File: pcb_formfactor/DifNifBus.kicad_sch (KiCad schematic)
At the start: 24 parts, among them J1 DBA-ESDI, U10 74LVC4245, U11 74LCX07, U12 74VHCT125, U14 74LVC4245, U6 74LVC4245, U7 74LVC4245, U8 74LVC4245, U9 74LVC4245

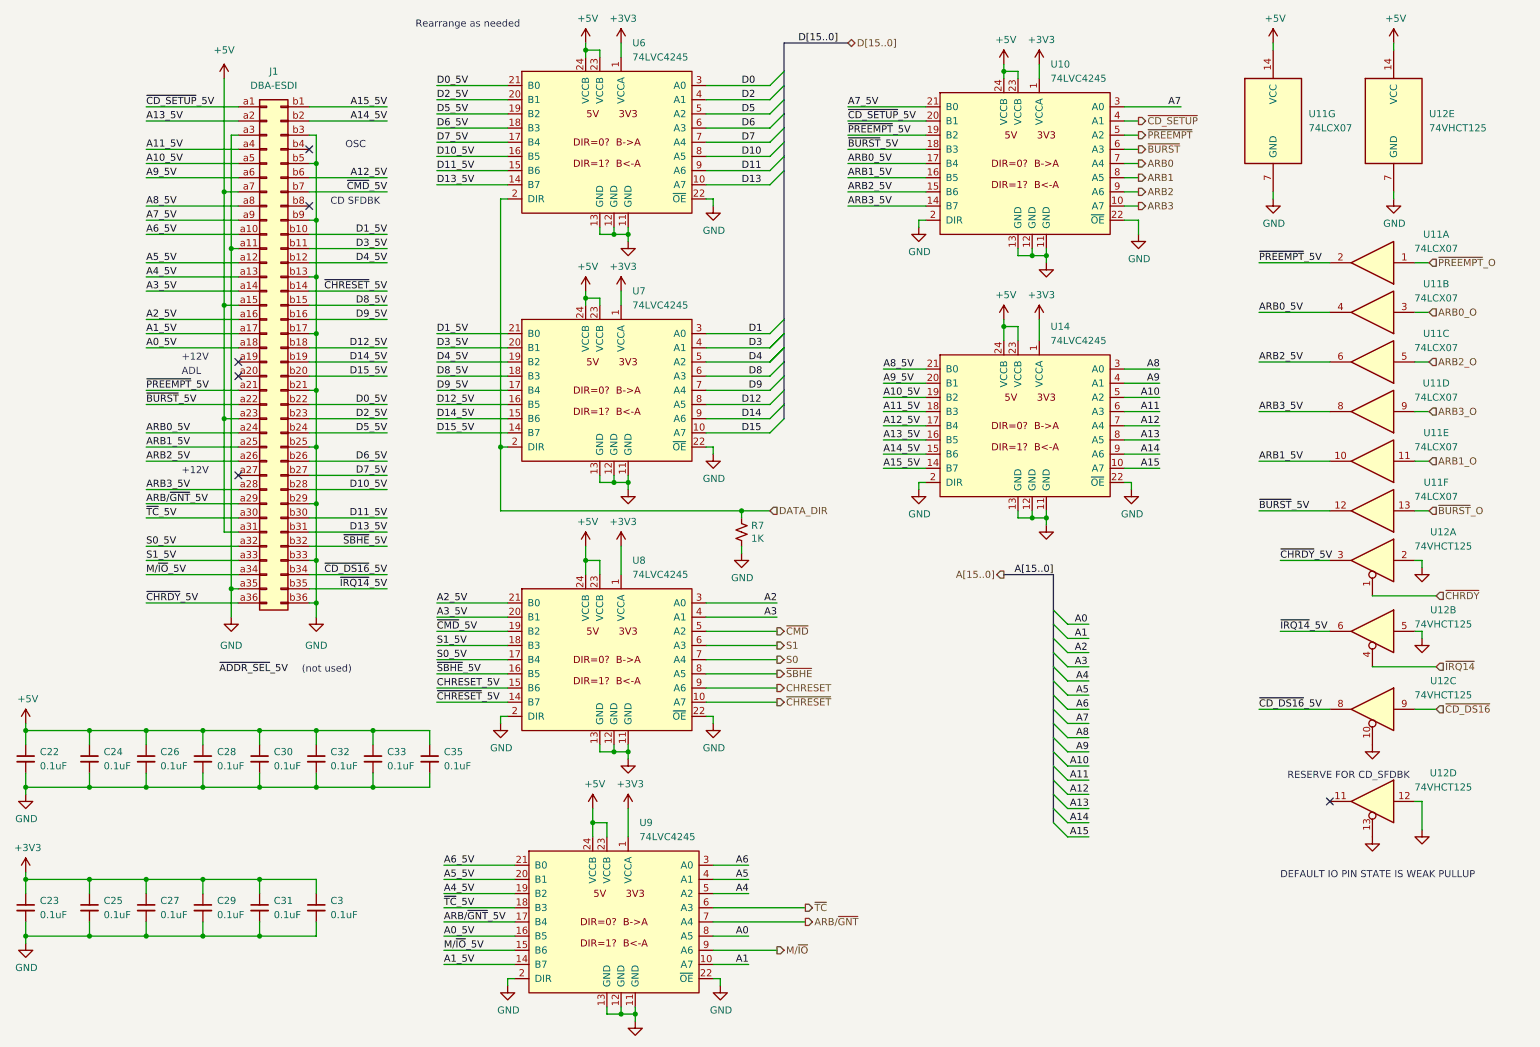
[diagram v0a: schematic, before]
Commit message: Add diode OR, add clock series R
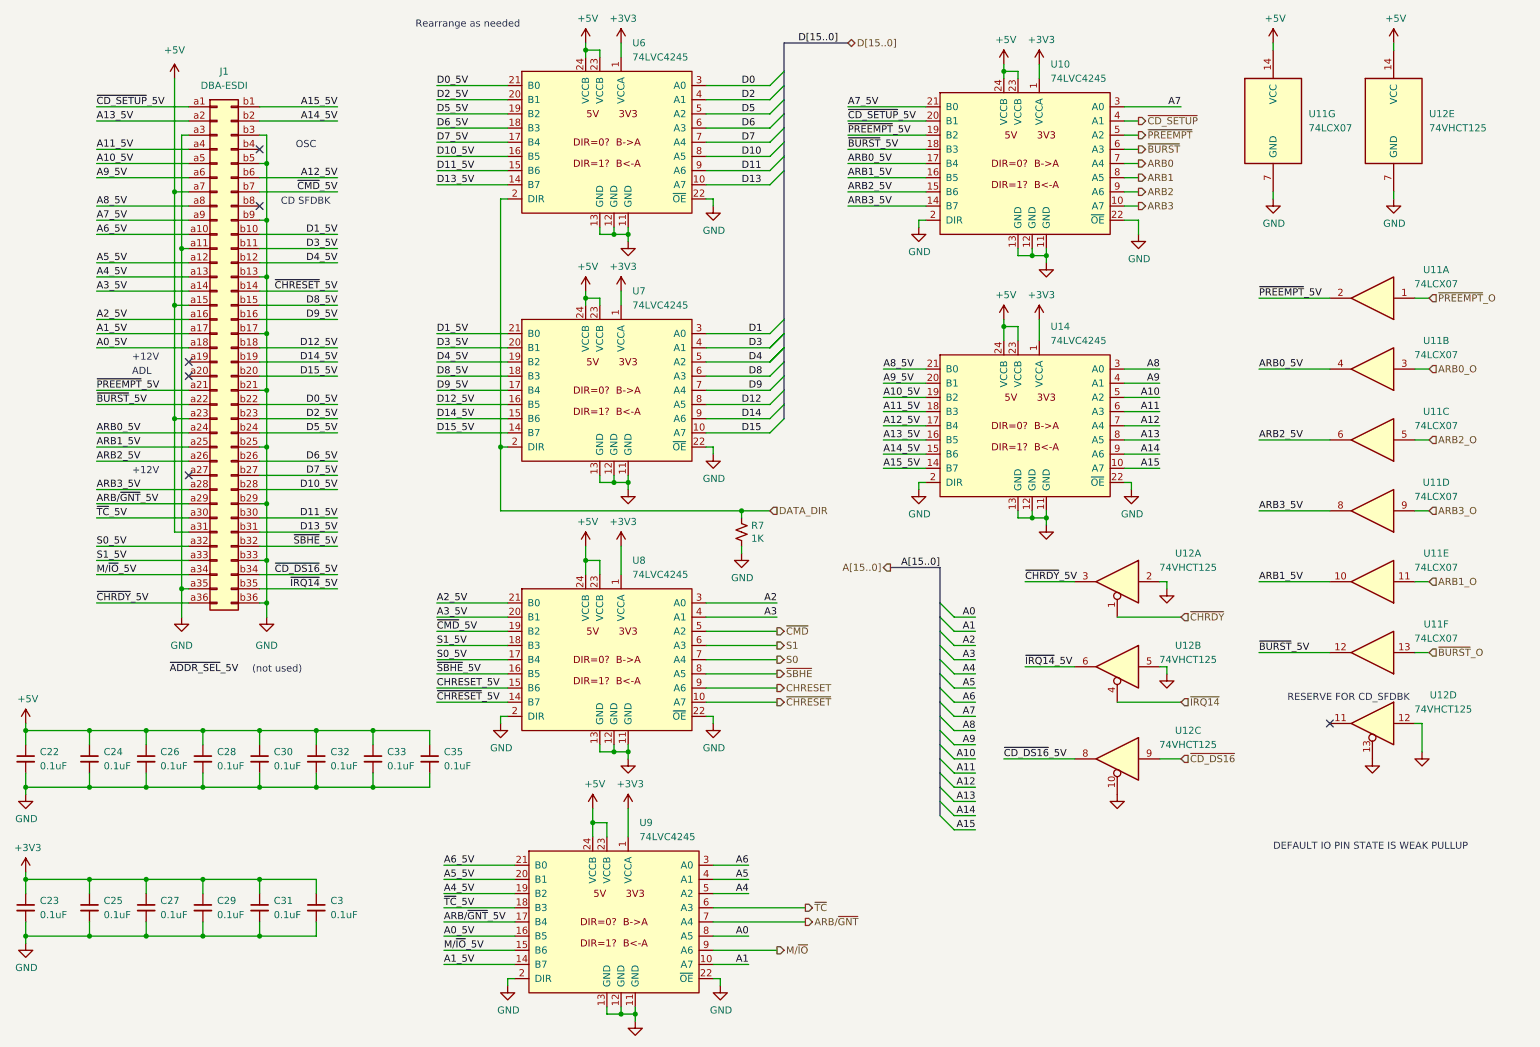
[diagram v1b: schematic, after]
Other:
- moved on the sheet: J1, U11A, U11B, U11C, U11D, U11E, U11F, U12A, U12B, U12C, U12D
